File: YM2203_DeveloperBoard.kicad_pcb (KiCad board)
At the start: 2 copper layers, 99.1 x 91.4 mm, 26 parts, among them J1 Conn_01x20_Pin, J2 Conn_01x20_Socket, J3 Conn_01x20_Socket, J4 Conn_01x20_Pin, J5 Conn_01x06_Socket, J6 AudioJack3, U3 MCP23S17_SP, U4 NJM4558, U5 NJM4558

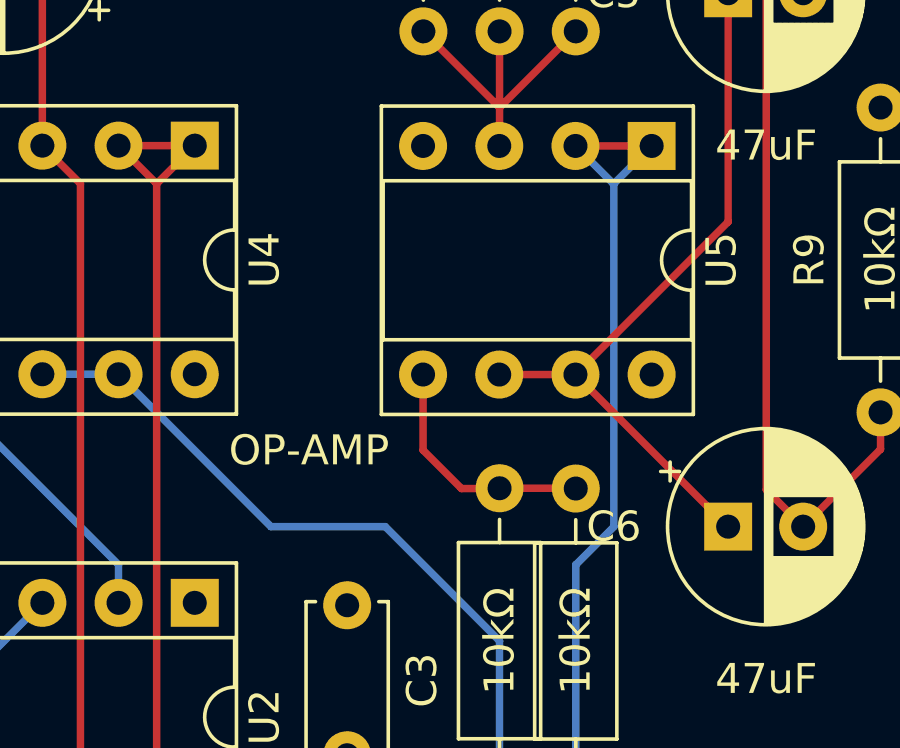
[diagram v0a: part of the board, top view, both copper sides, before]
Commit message: U5 の電源未配線を修正
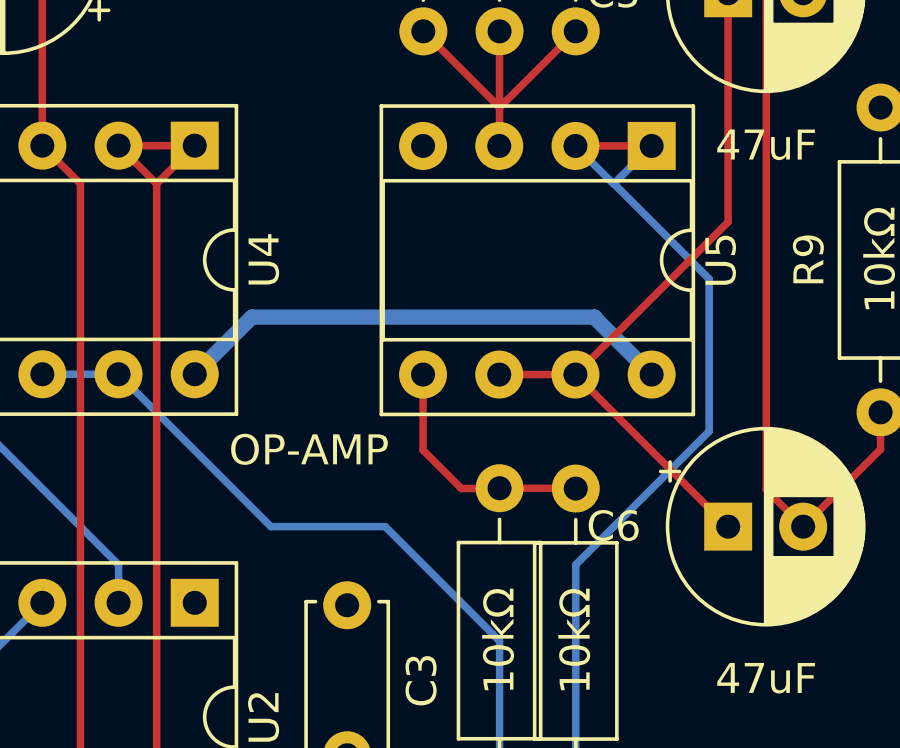
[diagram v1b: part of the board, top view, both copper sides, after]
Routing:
- net +5V: track 0.23 -> 17.1 mm
- net PSG_OUT: track 27.0 -> 29.6 mm
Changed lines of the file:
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@@
   (segment (start 159.94 127.08) (end 160.02 127) (width 0.25) (layer "F.Cu") (net 1))
   (segment (start 200.58 121.92) (end 200.66 122) (width 0.25) (layer "F.Cu") (net 1))
+  (segment (start 197.485 112.395) (end 195.58 114.3) (width 0.508) (layer "B.Cu") (net 1))
+  (segment (start 210.81 114.31) (end 208.915 112.415) (width 0.508) (layer "B.Cu") (net 1))
+  (segment (start 208.915 112.395) (end 197.485 112.395) (width 0.508) (layer "B.Cu") (net 1))
+  (segment (start 208.915 112.415) (end 208.915 112.395) (width 0.508) (layer "B.Cu") (net 1))
   (segment (start 134.62 119.38) (end 144.78 119.38) (width 0.25) (layer "F.Cu") (net 2))
   (segment (start 134.62 78.74) (end 144.78 78.74) (width 0.25) (layer "F.Cu") (net 2))
@@
   (segment (start 205.74 105.41) (end 208.28 102.87) (width 0.25) (layer "F.Cu") (net 47))
   (segment (start 208.27 106.69) (end 210.81 106.69) (width 0.25) (layer "F.Cu") (net 48))
+  (segment (start 212.725 116.205) (end 212.725 111.125) (width 0.25) (layer "B.Cu") (net 48))
   (segment (start 209.53 107.95) (end 208.27 106.69) (width 0.25) (layer "B.Cu") (net 48))
-  (segment (start 208.28 120.65) (end 209.55 119.38) (width 0.25) (layer "B.Cu") (net 48))
+  (segment (start 212.725 111.125) (end 209.55 107.95) (width 0.25) (layer "B.Cu") (net 48))
+  (segment (start 209.55 107.95) (end 210.81 106.69) (width 0.25) (layer "B.Cu") (net 48))
   (segment (start 208.28 128.27) (end 208.28 120.65) (width 0.25) (layer "B.Cu") (net 48))
-  (segment (start 209.55 107.95) (end 210.81 106.69) (width 0.25) (layer "B.Cu") (net 48))
-  (segment (start 209.55 119.38) (end 209.55 107.95) (width 0.25) (layer "B.Cu") (net 48))
+  (segment (start 208.28 120.65) (end 212.725 116.205) (width 0.25) (layer "B.Cu") (net 48))
   (segment (start 209.55 107.95) (end 209.53 107.95) (width 0.25) (layer "B.Cu") (net 48))
   (segment (start 205.75 118.1) (end 205.74 118.11) (width 0.25) (layer "F.Cu") (net 49))

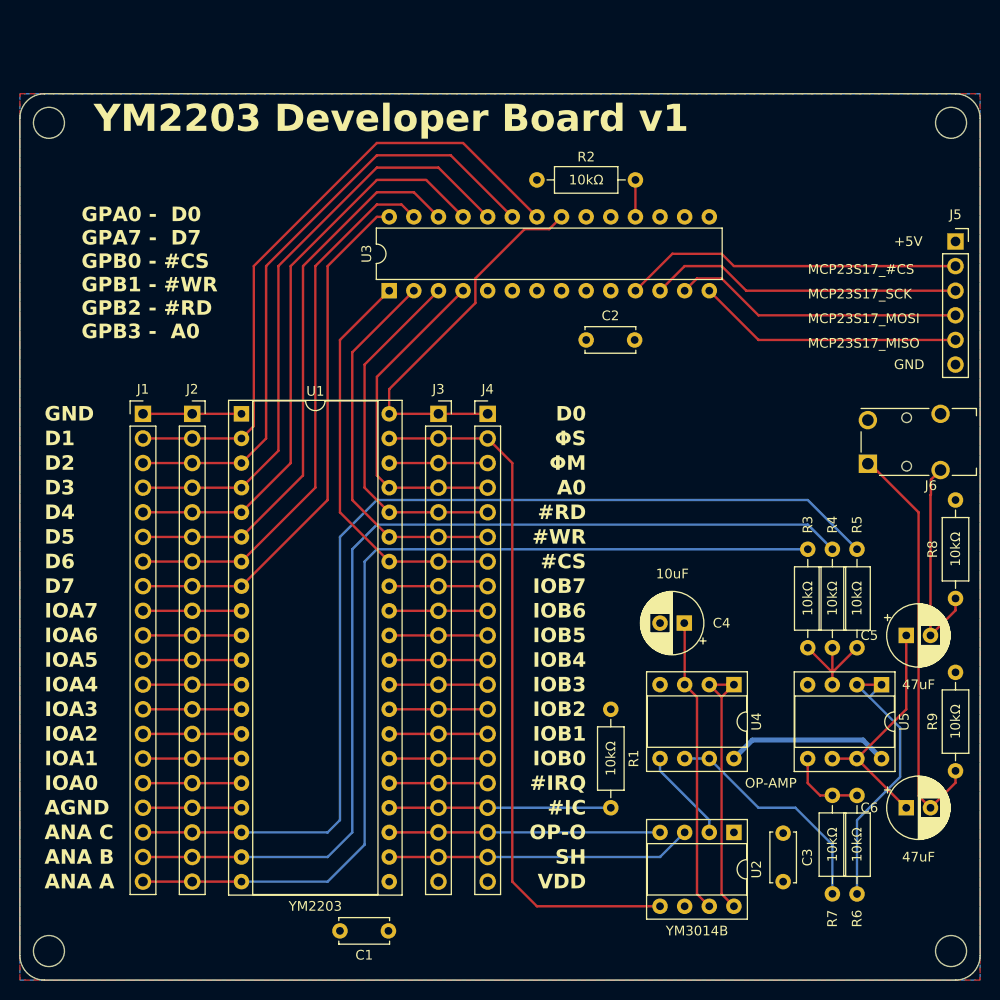
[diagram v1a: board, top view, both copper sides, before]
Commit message: 基板整形，シルク印刷追記修正
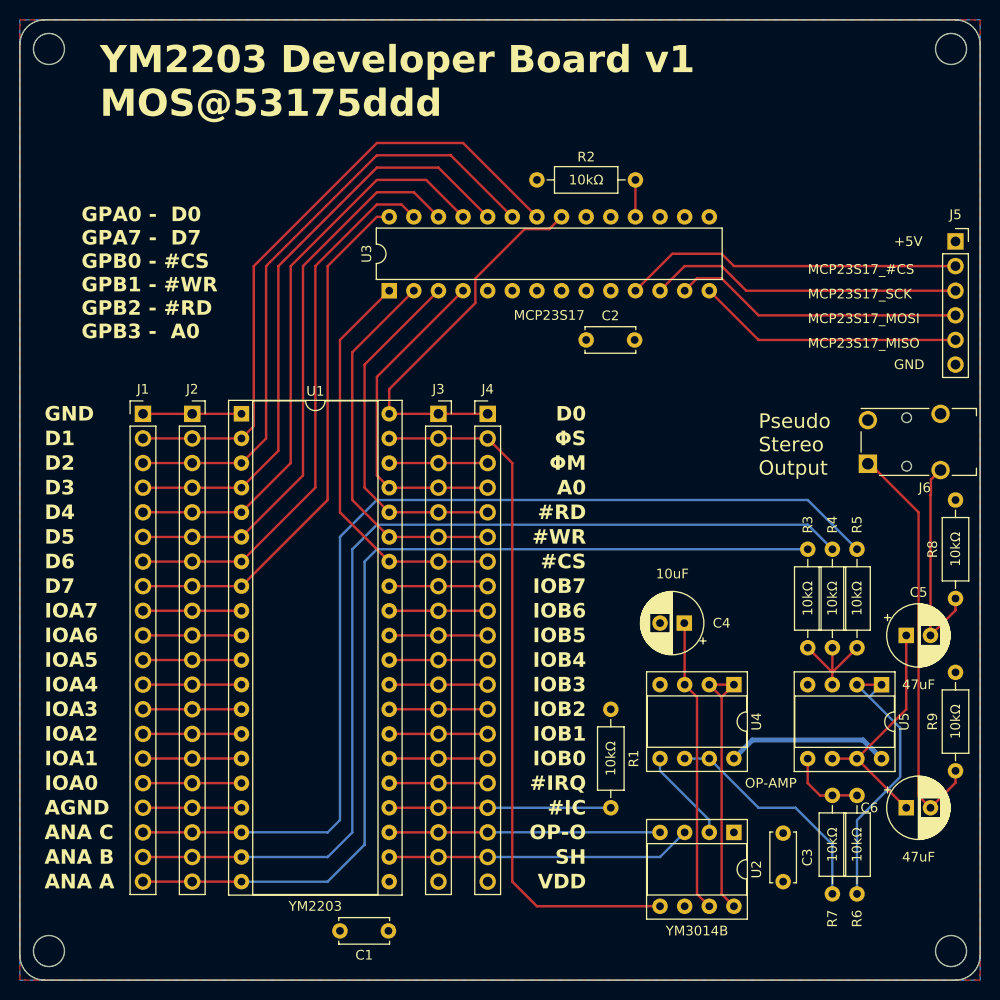
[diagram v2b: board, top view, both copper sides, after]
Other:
- board size 99.1 x 91.4 mm -> 99.1 x 99.1 mm
- board text added: "MCP23S17"
- board text added: "Pseudo Stereo Output"
- board text added: "YM2203 Developer Board v1 MOS@53175ddd"
- board text removed: "YM2203 Developer Board v1"
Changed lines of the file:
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@@
     (property "ki_keywords" "cap capacitor")
     (attr through_hole)
-    (fp_text reference "C5" (at -3.81 0) (layer "F.SilkS")
+    (fp_text reference "C5" (at 1.27 -4.445) (layer "F.SilkS")
         (effects (font (size 1 1) (thickness 0.15)))
     )
@@
     (property "ki_keywords" "audio jack receptacle stereo headphones phones TRS connector")
     (attr through_hole)
-    (fp_text reference "J6" (at 0 -4.5) (layer "F.SilkS")
+    (fp_text reference "J6" (at 0.635 -4.72) (layer "F.SilkS")
         (effects (font (size 1 1) (thickness 0.15)))
     )
@@
     )
   )
-  (gr_line (start 127.92 45.72) (end 121.92 51.72)
+  (gr_line (start 127.92 38.1) (end 121.92 44.1)
     (stroke (width 0.15) (type default)) (layer "Dwgs.User"))
   (gr_line (start 121.92 131.16) (end 127.92 137.16)
     (stroke (width 0.15) (type default)) (layer "Dwgs.User"))
-  (gr_line (start 220.98 45.72) (end 214.98 51.72)
+  (gr_line (start 220.98 38.1) (end 214.98 44.1)
     (stroke (width 0.15) (type default)) (layer "Dwgs.User"))
-  (gr_line (start 121.92 45.72) (end 127.92 51.72)
+  (gr_line (start 121.92 38.1) (end 127.92 44.1)
     (stroke (width 0.15) (type default)) (layer "Dwgs.User"))
-  (gr_line (start 220.98 51.72) (end 214.98 45.72)
+  (gr_line (start 220.98 44.1) (end 214.98 38.1)
     (stroke (width 0.15) (type default)) (layer "Dwgs.User"))
   (gr_line (start 220.98 137.16) (end 214.98 131.16)
@@
   (gr_arc (start 124.46 137.16) (mid 122.663949 136.416051) (end 121.92 134.62)
     (stroke (width 0.1) (type default)) (layer "Edge.Cuts"))
-  (gr_line (start 121.92 48.26) (end 121.92 134.62)
+  (gr_line (start 121.92 40.64) (end 121.92 134.62)
     (stroke (width 0.1) (type default)) (layer "Edge.Cuts"))
-  (gr_line (start 220.98 134.62) (end 220.98 48.26)
+  (gr_line (start 220.98 134.62) (end 220.98 40.64)
     (stroke (width 0.1) (type default)) (layer "Edge.Cuts"))
   (gr_circle (center 217.98 134.16) (end 216.38 134.16)
     (stroke (width 0.1) (type default)) (fill none) (layer "Edge.Cuts"))
-  (gr_circle (center 217.98 48.72) (end 217.98 50.32)
+  (gr_circle (center 217.98 41.1) (end 217.98 42.7)
     (stroke (width 0.1) (type default)) (fill none) (layer "Edge.Cuts"))
-  (gr_arc (start 121.92 48.26) (mid 122.663949 46.463949) (end 124.46 45.72)
+  (gr_arc (start 121.92 40.64) (mid 122.663949 38.843949) (end 124.46 38.1)
     (stroke (width 0.1) (type default)) (layer "Edge.Cuts"))
-  (gr_circle (center 124.92 48.72) (end 126.52 48.72)
+  (gr_circle (center 124.92 41.1) (end 126.52 41.1)
     (stroke (width 0.1) (type default)) (fill none) (layer "Edge.Cuts"))
   (gr_arc (start 220.98 134.62) (mid 220.236051 136.416051) (end 218.44 137.16)
     (stroke (width 0.1) (type default)) (layer "Edge.Cuts"))
-  (gr_line (start 218.44 45.72) (end 124.46 45.72)
+  (gr_line (start 218.44 38.1) (end 124.46 38.1)
     (stroke (width 0.1) (type default)) (layer "Edge.Cuts"))
-  (gr_arc (start 218.44 45.72) (mid 220.236051 46.463949) (end 220.98 48.26)
+  (gr_arc (start 218.44 38.1) (mid 220.236051 38.843949) (end 220.98 40.64)
     (stroke (width 0.1) (type default)) (layer "Edge.Cuts"))
   (gr_line (start 124.46 137.16) (end 218.44 137.16)
@@
     (effects (font (size 1 1) (thickness 0.15)))
   )
+  (gr_text "MCP23S17" (at 176.53 68.58) (layer "F.SilkS")
+    (effects (font (size 1 1) (thickness 0.15)))
+  )
   (gr_text "GPA0 -  D0\nGPA7 -  D7\nGPB0 - #CS\nGPB1 - #WR\nGPB2 - #RD\nGPB3 -  A0" (at 128.27 71.12) (layer "F.SilkS")
     (effects (font (size 1.5 1.5) (thickness 0.3) bold) (justify left bottom))
@@
     (effects (font (size 1 1) (thickness 0.15)) (justify left))
   )
-  (gr_text "YM2203 Developer Board v1" (at 129.54 48.26) (layer "F.SilkS")
+  (gr_text "YM2203 Developer Board v1\nMOS@53175ddd" (at 130.175 44.45) (layer "F.SilkS")
     (effects (font (size 2.8 2.8) (thickness 0.3) bold) (justify left))
   )
@@
     (effects (font (size 1.5 1.5) (thickness 0.3) bold) (justify right))
   )
+  (gr_text "Pseudo\nStereo\nOutput" (at 198.12 81.915) (layer "F.SilkS")
+    (effects (font (size 1.5 1.5) (thickness 0.2)) (justify left))
+  )
   (gr_text "IOB1" (at 180.34 111.76) (layer "F.SilkS")
     (effects (font (size 1.5 1.5) (thickness 0.3) bold) (justify right))
@@
   )
   (dimension (type aligned) (layer "Dwgs.User")
-    (pts (xy 220.98 137.16) (xy 220.98 45.72))
+    (pts (xy 220.98 137.16) (xy 220.98 38.1))
     (height 6.35)
-    (gr_text "91.4400 mm" (at 226.18 91.44 90) (layer "Dwgs.User")
+    (gr_text "99.0600 mm" (at 226.18 87.63 90) (layer "Dwgs.User")
       (effects (font (size 1 1) (thickness 0.15)))
     )
@@
     (polygon
       (pts
-        (xy 220.98 45.72)
+        (xy 220.98 38.1)
         (xy 220.98 137.16)
         (xy 121.92 137.16)
-        (xy 121.92 45.72)
+        (xy 121.92 38.1)
       )
     )
@@
     (polygon
       (pts
-        (xy 121.92 45.72)
+        (xy 121.92 38.1)
         (xy 121.92 137.16)
         (xy 220.98 137.16)
-        (xy 220.98 45.72)
+        (xy 220.98 38.1)
       )
     )

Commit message: v2
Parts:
- added U6: ~, Package_TO_SOT_THT:TO-92_Inline_Wide, F.Cu at (184.2, 83.8)
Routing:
- net +5V: track 17.1 -> 0.23 mm
- net OPN_ΦM: track 10.2 -> 24.1 mm
- net GND: track 20.3 -> 10.2 mm
- net Net-(U5B--): track 24.5 -> 27.5 mm
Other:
- board text added: "1MHz"
- board text added: "YM2203 Developer Board v2 MOS@53175ddd"
- board text removed: "YM2203 Developer Board v1 MOS@53175ddd"
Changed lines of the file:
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@@
+    )
+  )
+  (footprint "Package_TO_SOT_THT:TO-92_Inline_Wide" (layer "F.Cu")
+    (at 184.15 83.82)
+    (descr "TO-92 leads in-line, wide, drill 0.75mm (see NXP sot054_po.pdf)")
+    (tags "to-92 sc-43 sc-43a sot54 PA33 transistor")
+    (property "Sheetfile" "YM2203_DeveloperBoard.kicad_sch")
+    (property "Sheetname" "")
+    (attr through_hole)
+    (fp_text reference "U6" (at 2.54 -3.56) (layer "F.SilkS")
+        (effects (font (size 1 1) (thickness 0.15)))
+    )
+    (fp_text value "~" (at 2.54 2.79) (layer "F.Fab")
+        (effects (font (size 1 1) (thickness 0.15)))
+    )
+    (fp_text user "${REFERENCE}" (at 2.54 0) (layer "F.Fab")
+        (effects (font (size 1 1) (thickness 0.15)))
+    )
+    (fp_line (start 0.74 1.85) (end 4.34 1.85)
+      (stroke (width 0.12) (type solid)) (layer "F.SilkS"))
+    (fp_arc (start 0.1836 -1.098807) (mid 1.143021 -2.192817) (end 2.54 -2.6)
+      (stroke (width 0.12) (type solid)) (layer "F.SilkS"))
+    (fp_arc (start 0.74 1.85) (mid 0.446097 1.509328) (end 0.215816 1.122795)
+      (stroke (width 0.12) (type solid)) (layer "F.SilkS"))
+    (fp_arc (start 2.54 -2.6) (mid 3.936979 -2.192818) (end 4.8964 -1.098807)
+      (stroke (width 0.12) (type solid)) (layer "F.SilkS"))
+    (fp_arc (start 4.864184 1.122795) (mid 4.633903 1.509328) (end 4.34 1.85)
+      (stroke (width 0.12) (type solid)) (layer "F.SilkS"))
+    (fp_line (start -1.01 -2.73) (end -1.01 2.01)
+      (stroke (width 0.05) (type solid)) (layer "F.CrtYd"))
+    (fp_line (start -1.01 -2.73) (end 6.09 -2.73)
+      (stroke (width 0.05) (type solid)) (layer "F.CrtYd"))
+    (fp_line (start 6.09 2.01) (end -1.01 2.01)
+      (stroke (width 0.05) (type solid)) (layer "F.CrtYd"))
+    (fp_line (start 6.09 2.01) (end 6.09 -2.73)
+      (stroke (width 0.05) (type solid)) (layer "F.CrtYd"))
+    (fp_line (start 0.8 1.75) (end 4.3 1.75)
+      (stroke (width 0.1) (type solid)) (layer "F.Fab"))
+    (fp_arc (start 0.786375 1.753625) (mid 0.248779 -0.949055) (end 2.54 -2.48)
+      (stroke (width 0.1) (type solid)) (layer "F.Fab"))
+    (fp_arc (start 2.54 -2.48) (mid 4.831221 -0.949055) (end 4.293625 1.753625)
+      (stroke (width 0.1) (type solid)) (layer "F.Fab"))
+    (pad "1" thru_hole rect (at 0 0) (size 1.5 1.5) (drill 0.8) (layers "*.Cu" "*.Mask")
+      (net 25 "OPN_ΦM") (pinfunction "OUT") (pintype "output"))
+    (pad "2" thru_hole circle (at 2.54 0) (size 1.5 1.5) (drill 0.8) (layers "*.Cu" "*.Mask")
+      (net 2 "GND") (pinfunction "GND") (pintype "power_in"))
+    (pad "3" thru_hole circle (at 5.08 0) (size 1.5 1.5) (drill 0.8) (layers "*.Cu" "*.Mask")
+      (net 1 "+5V") (pinfunction "Vcc") (pintype "power_in"))
+    (model "${KICAD6_3DMODEL_DIR}/Package_TO_SOT_THT.3dshapes/TO-92_Inline_Wide.wrl"
+      (offset (xyz 0 0 0))
+      (scale (xyz 1 1 1))
+      (rotate (xyz 0 0 0))
     )
   )
@@
     (effects (font (size 1.5 1.5) (thickness 0.3) bold) (justify right))
   )
+  (gr_text "1MHz" (at 186.69 86.36) (layer "F.SilkS")
+    (effects (font (size 1.5 1.5) (thickness 0.2)) (justify top))
+  )
   (gr_text "IOA1" (at 124.46 114.3) (layer "F.SilkS")
     (effects (font (size 1.5 1.5) (thickness 0.3) bold) (justify left))
@@
     (effects (font (size 1 1) (thickness 0.15)) (justify left))
   )
-  (gr_text "YM2203 Developer Board v1\nMOS@53175ddd" (at 130.175 44.45) (layer "F.SilkS")
+  (gr_text "YM2203 Developer Board v2\nMOS@53175ddd" (at 130.175 44.45) (layer "F.SilkS")
     (effects (font (size 2.8 2.8) (thickness 0.3) bold) (justify left))
   )
@@
   (segment (start 159.94 127.08) (end 160.02 127) (width 0.25) (layer "F.Cu") (net 1))
   (segment (start 200.58 121.92) (end 200.66 122) (width 0.25) (layer "F.Cu") (net 1))
-  (segment (start 197.485 112.395) (end 195.58 114.3) (width 0.508) (layer "B.Cu") (net 1))
-  (segment (start 210.81 114.31) (end 208.915 112.415) (width 0.508) (layer "B.Cu") (net 1))
-  (segment (start 208.915 112.395) (end 197.485 112.395) (width 0.508) (layer "B.Cu") (net 1))
-  (segment (start 208.915 112.415) (end 208.915 112.395) (width 0.508) (layer "B.Cu") (net 1))
   (segment (start 134.62 119.38) (end 144.78 119.38) (width 0.25) (layer "F.Cu") (net 2))
-  (segment (start 134.62 78.74) (end 144.78 78.74) (width 0.25) (layer "F.Cu") (net 2))
   (segment (start 190.5 100.37) (end 190.46 100.33) (width 0.25) (layer "F.Cu") (net 3))
   (segment (start 191.77 107.95) (end 191.77 128.27) (width 0.25) (layer "F.Cu") (net 3))
@@
   (segment (start 208.27 114.31) (end 213.36 109.22) (width 0.25) (layer "F.Cu") (net 4))
   (segment (start 213.36 109.22) (end 213.36 101.6) (width 0.25) (layer "F.Cu") (net 4))
-  (segment (start 208.27 114.31) (end 213.34 119.38) (width 0.25) (layer "F.Cu") (net 4))
   (segment (start 213.34 119.38) (end 213.36 119.38) (width 0.25) (layer "F.Cu") (net 4))
   (segment (start 205.73 114.31) (end 208.27 114.31) (width 0.25) (layer "F.Cu") (net 4))
+  (segment (start 213.36 109.22) (end 213.36 119.38) (width 0.25) (layer "F.Cu") (net 4))
   (segment (start 144.78 81.28) (end 146.05 80.01) (width 0.25) (layer "F.Cu") (net 5))
   (segment (start 146.05 80.01) (end 146.05 63.5) (width 0.25) (layer "F.Cu") (net 5))
@@
   (segment (start 160.02 81.28) (end 170.18 81.28) (width 0.25) (layer "F.Cu") (net 24))
   (segment (start 160.02 83.82) (end 170.18 83.82) (width 0.25) (layer "F.Cu") (net 25))
+  (segment (start 184.15 83.82) (end 170.18 83.82) (width 0.25) (layer "B.Cu") (net 25))
   (segment (start 158.75 85.09) (end 158.75 74.93) (width 0.25) (layer "F.Cu") (net 26))
   (segment (start 158.75 74.93) (end 167.64 66.04) (width 0.25) (layer "F.Cu") (net 26))
